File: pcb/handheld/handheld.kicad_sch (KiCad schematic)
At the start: 0 parts

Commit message: Picked some components
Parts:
- added J1: USB_C_Receptacle, symbol Connector:USB_C_Receptacle
- added U1: ESP32-S3-WROOM-1, RF_Module:ESP32-S3-WROOM-1, symbol RF_Module:ESP32-S3-WROOM-1
- added U2: AMS1117-3.3, Package_TO_SOT_SMD:SOT-223-3_TabPin2, symbol Regulator_Linear:AMS1117-3.3
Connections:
- new net: U1.1 (GND), U1.40 (GND), U1.41 (GND)
- new net: J1.A1 (GND), J1.A12 (GND), J1.B1 (GND), J1.B12 (GND)
- new net: J1.A4 (VBUS), J1.A9 (VBUS), J1.B4 (VBUS), J1.B9 (VBUS)

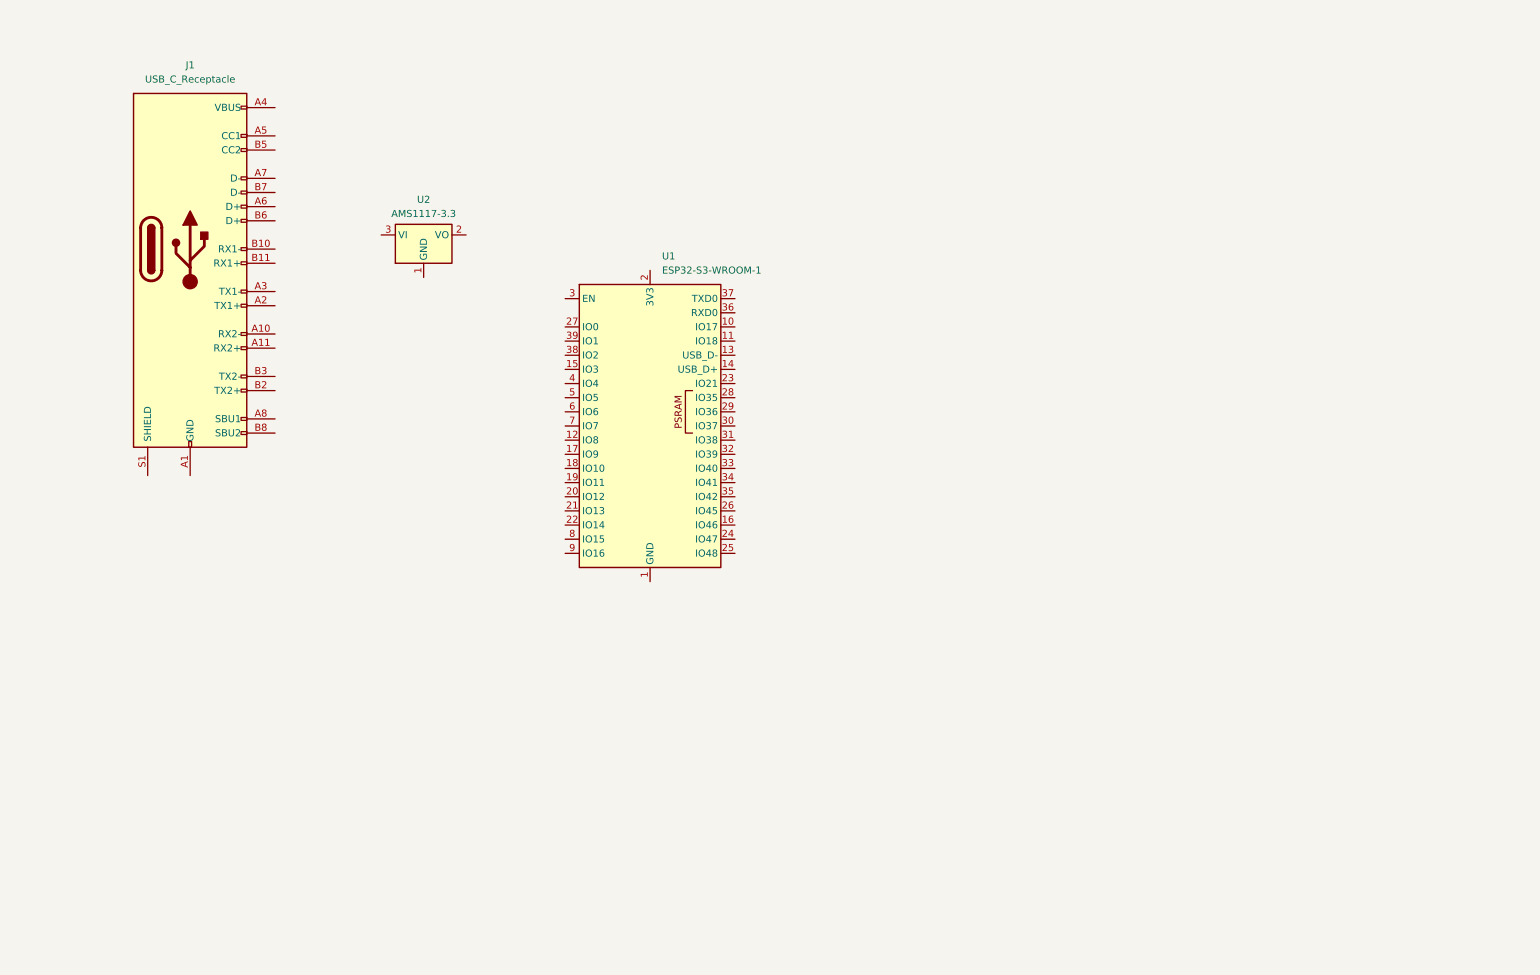
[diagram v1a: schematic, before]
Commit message: Added stuff from website
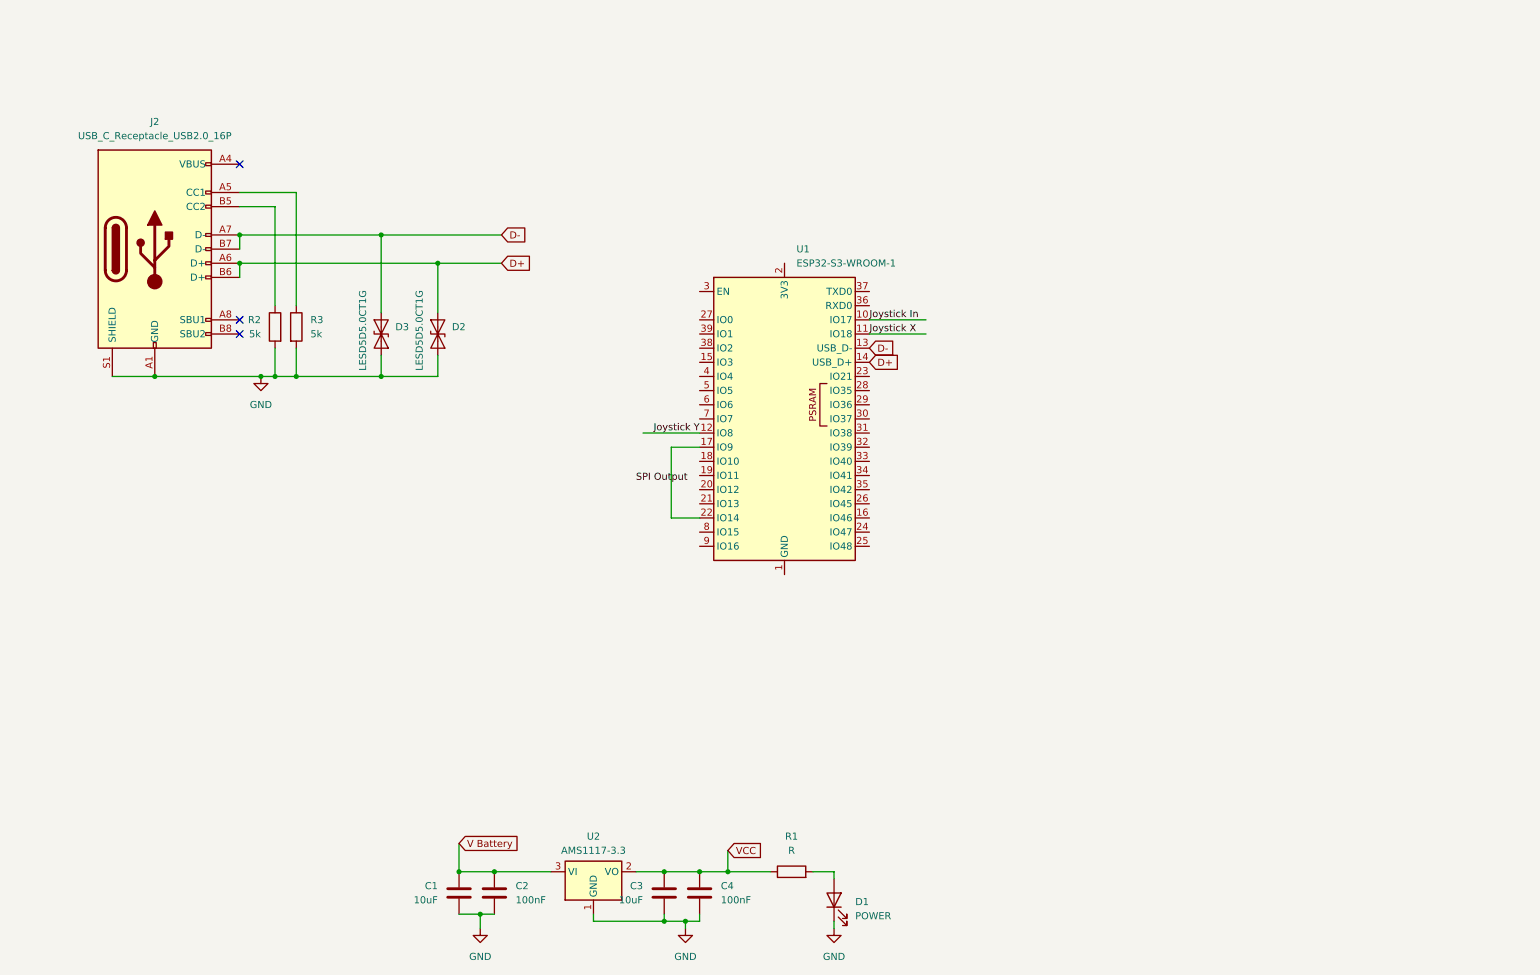
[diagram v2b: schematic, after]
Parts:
- removed J1: USB_C_Receptacle, symbol Connector:USB_C_Receptacle
- added C1, C3: 10uF, symbol Device:C
- added C2, C4: 100nF, symbol Device:C
- added D1: POWER, symbol Device:LED
- added D2, D3: LESD5D5.0CT1G, Diode_SMD:D_SOD-523, symbol Diode:ESD131-B1-W0201
- added J2: USB_C_Receptacle_USB2.0_16P, symbol Connector:USB_C_Receptacle_USB2.0_16P
- added R1: R, symbol Device:R
- added R2, R3: 5k, symbol Device:R
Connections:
- net Joystick In: now reaches U1.10 (IO17)
- net Joystick X: now reaches U1.11 (IO18)
- net Joystick Y: now reaches U1.12 (IO8)
- net D-: now reaches U1.13 (USB_D-)
- net D-: now also D3.2 (A2), J2.A7 (D-), J2.B7 (D-)
- net D+: now reaches U1.14 (USB_D+)
- net D+: now also D2.2 (A2), J2.A6 (D+), J2.B6 (D+)
- net at U1.17 (IO9): now also U1.22 (IO14)
- net GND: now reaches U2.1 (GND)
- net GND: now also C1.2, C2.2, C3.2, C4.2, D1.1 (K), D2.1 (A1), D3.1 (A1), J2.A1 (GND), J2.A12 (GND), J2.B1 (GND), J2.B12 (GND), J2.S1 (SHIELD), R2.2, R3.2
- net VCC: now reaches U2.2 (VO)
- net VCC: now also C3.1, C4.1, R1.1
- net V Battery: now reaches U2.3 (VI)
- net V Battery: now also C1.1, C2.1
- new net: J2.A5 (CC1), R3.1
- new net: D1.2 (A), R1.2
- new net: J2.A4 (VBUS), J2.A9 (VBUS), J2.B4 (VBUS), J2.B9 (VBUS)
- new net: J2.B5 (CC2), R2.1
- no-connect marks 0 -> 3
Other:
- moved on the sheet: U1, U2

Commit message: Update handheld.kicad_sch
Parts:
- added C5: 10uF, symbol Device:C
- added C6, C8, C9: 100nF, symbol Device:C
- added C7: 1uF, symbol Device:C
- added J1: Display Output, symbol Connector_Generic:Conn_01x14
- added R4, R6: R, symbol Device:R
- added R5: 10k, symbol Device:R
- added SW1: PLACEHOLDER, Button_Switch_SMD:Nidec_Copal_CAS-120A, symbol Switch:SW_Nidec_CAS-120A1
- added SW2, SW3: SW_Push, symbol Switch:SW_Push
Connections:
- net GND: now also U1.1 (GND), U1.40 (GND), U1.41 (GND), C5.2, C6.2, C7.2, C8.2, C9.2, J1.2 (Pin_2), R4.1, SW2.2, SW3.2
- net V Battery: now also SW1.3 (A); no longer C1.1, C2.1, U2.3 (VI)
- net VCC: now also U1.2 (3V3), C5.1, C6.1, J1.1 (Pin_1), R5.1, R6.1
- net at U1.17 (IO9): no longer U1.22 (IO14)
- net CS: now reaches U1.18 (IO10)
- net CS: now also J1.3 (Pin_3)
- net SDI(MOSI): now reaches U1.19 (IO11)
- net SDI(MOSI): now also J1.6 (Pin_6)
- net SCK: now reaches U1.20 (IO12)
- net SCK: now also J1.7 (Pin_7)
- net SDO(MISO): now reaches U1.21 (IO13)
- net SDO(MISO): now also J1.9 (Pin_9)
- net BOOT: now reaches U1.27 (IO0)
- net BOOT: now also C9.1, R6.2, SW3.1
- net RESET: now reaches U1.3 (EN)
- net RESET: now also C7.1, C8.1, J1.4 (Pin_4), R5.2, SW2.1
- new net: R4.2, SW1.1 (C)
- new net: C1.1, C2.1, SW1.2 (B), U2.3 (VI)
- new net DC/RS: J1.5 (Pin_5)
- new net LED: J1.8 (Pin_8)
- new net T_CLK: J1.10 (Pin_10)
- new net T_CS: J1.11 (Pin_11)
- new net T_DIN: J1.12 (Pin_12)
- new net T_DO: J1.13 (Pin_13)
- new net T_IRQ: J1.14 (Pin_14)
- no-connect marks 3 -> 8

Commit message: Schematic mostly done???
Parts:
- added J3: Speaker ~(3W, 8R), symbol Connector_Generic:Conn_01x02
- added J4: UART (Just in case?), symbol Connector_Generic:Conn_01x02
- added Q1: MMBT3904, Package_TO_SOT_SMD:SOT-23, symbol Transistor_BJT:MMBT3904
- added R7: R_Variable ~1k, symbol Device:R_Variable
- added R8: 10k, symbol Device:R
- added R9: 330, symbol Device:R
- added SW4: Push Button, symbol Switch:SW_Push
- R6: value R -> 10k
- SW2: value SW_Push -> Reset Button
- SW3: value SW_Push -> Boot Button
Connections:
- net DC/RS: now also U1.22 (IO14)
- net GND: now also J3.2 (Pin_2), Q1.2 (E), R8.2
- net LED: now also U1.7 (IO7)
- net RESET: now also U1.17 (IO9)
- net T_CLK: now also U1.23 (IO21)
- net T_CS: now also U1.9 (IO16)
- net T_DIN: now also U1.24 (IO47)
- net T_DO: now also U1.25 (IO48)
- net T_IRQ: now also U1.8 (IO15)
- net VCC: now also SW4.2
- net Speaker: now reaches U1.31 (IO38)
- net Speaker: now also R7.2
- net at U1.36 (RXD0): now also J4.2 (Pin_2)
- net at U1.37 (TXD0): now also J4.1 (Pin_1)
- new net: Q1.1 (B), R7.1
- new net: R8.1, R9.1, SW4.1
- new net: J3.1 (Pin_1), Q1.3 (C)
- new net BUTTON 1: R9.2
- no-connect marks 8 -> 9
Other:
- note added: "Generic Button Layout"

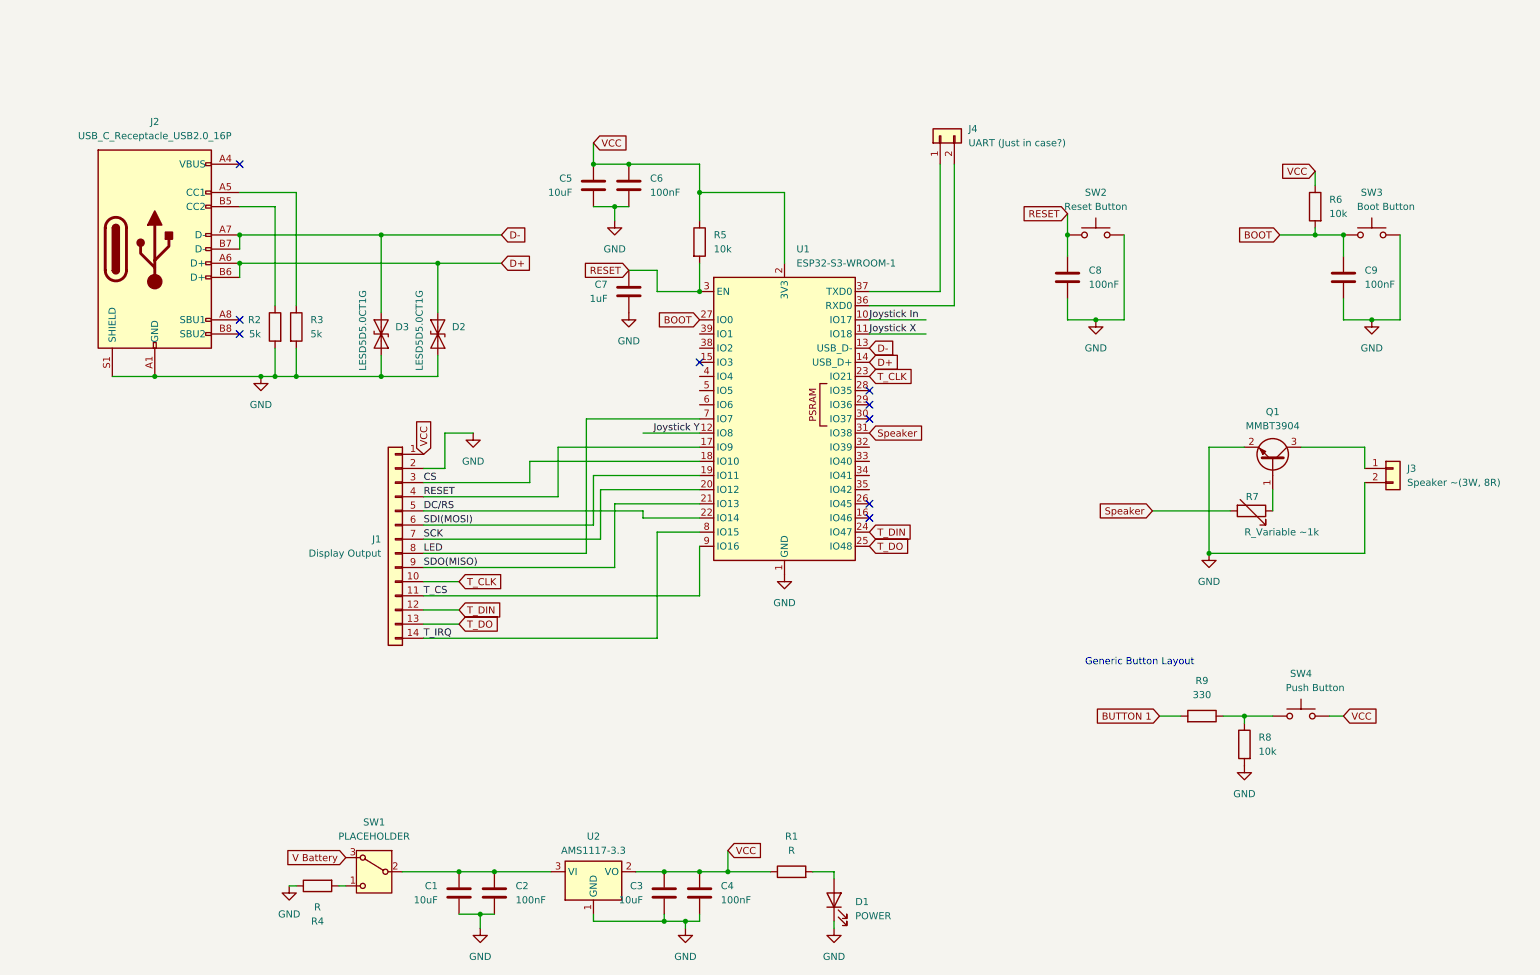
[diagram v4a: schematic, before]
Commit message: Assigned pins and finished schematic draft
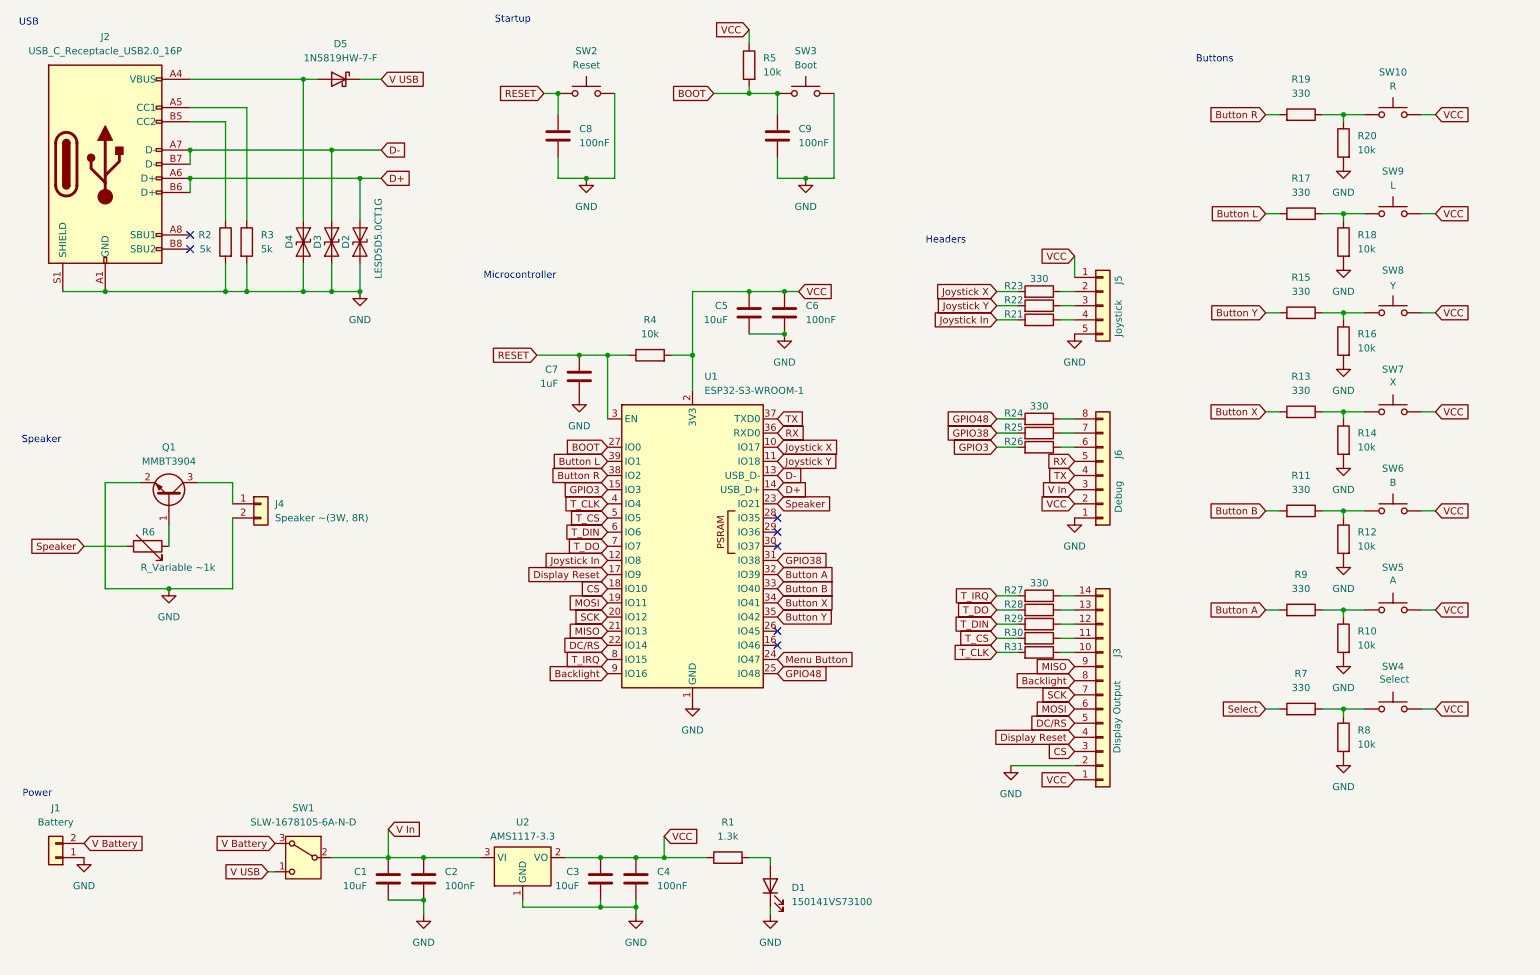
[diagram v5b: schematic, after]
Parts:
- removed J4: UART (Just in case?), symbol Connector_Generic:Conn_01x02
- removed R4: R, symbol Device:R
- added D4: LESD5D5.0CT1G, Diode_SMD:D_SOD-523, symbol Diode:ESD131-B1-W0201
- added D5: 1N5819HW-7-F, Diode_THT:D_DO-41_SOD81_P10.16mm_Horizontal, symbol Diode:1N5819
- added J1: Battery, symbol Connector_Generic:Conn_01x02
- added J5: Joystick, symbol Connector_Generic:Conn_01x05
- added J6: Debug, symbol Connector_Generic:Conn_01x08
- added R10, R12, R14, R16, R18, R20: 10k, symbol Device:R
- added R11, R13, R15, R17, R19, R21, R22, R23, R24, R25, R26, R27, R28, R29, R30, R31, R9: 330, symbol Device:R
- added SW10: R, symbol Switch:SW_Push
- added SW5: A, symbol Switch:SW_Push
- added SW6: B, symbol Switch:SW_Push
- added SW7: X, symbol Switch:SW_Push
- added SW8: Y, symbol Switch:SW_Push
- added SW9: L, symbol Switch:SW_Push
- D1: value POWER -> 150141VS73100
- R1: value R -> 1.3k
- SW1: value PLACEHOLDER -> SLW-1678105-6A-N-D
- SW2: value Reset Button -> Reset
- SW3: value Boot Button -> Boot
- SW4: value Push Button -> Select
- renumbered J1 to J3, J3 to J4, R5 to R4, R6 to R5, R7 to R6, R9 to R7
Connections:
- net GND: now also D4.1 (A1), J1.1 (Pin_1), J5.5 (Pin_5), J6.1 (Pin_1), R10.2, R12.2, R14.2, R16.2, R18.2, R20.2
- net Joystick In: now also U1.12 (IO8), R21.2; no longer U1.10 (IO17)
- net Joystick X: now also U1.10 (IO17), R23.2; no longer U1.11 (IO18)
- net Joystick Y: now also U1.11 (IO18), R22.2; no longer U1.12 (IO8)
- net RESET: now also R4.1; no longer J3.4 (Pin_4), R4.2, U1.17 (IO9)
- net Speaker: now also U1.23 (IO21); no longer U1.31 (IO38)
- net T_CLK: now also U1.4 (IO4), R31.2; no longer J3.10 (Pin_10), U1.23 (IO21)
- net T_CS: now also U1.5 (IO5), R30.2; no longer J3.11 (Pin_11), U1.9 (IO16)
- net T_DIN: now also U1.6 (IO6), R29.2; no longer J3.12 (Pin_12), U1.24 (IO47)
- net T_DO: now also U1.7 (IO7), R28.2; no longer J3.13 (Pin_13), U1.25 (IO48)
- net T_IRQ: now also R27.2; no longer J3.14 (Pin_14)
- net V Battery: now also J1.2 (Pin_2)
- net VCC: now also R4.2, J5.1 (Pin_1), J6.2 (Pin_2), SW10.2, SW5.2, SW6.2, SW7.2, SW8.2, SW9.2; no longer R4.1
- net GPIO3: now reaches U1.15 (IO3)
- net GPIO3: now also R26.2
- net Button A: now reaches U1.32 (IO39)
- net Button A: now also R9.2
- net Button B: now reaches U1.33 (IO40)
- net Button B: now also R11.2
- net Button X: now reaches U1.34 (IO41)
- net Button X: now also R13.2
- net Button Y: now reaches U1.35 (IO42)
- net Button Y: now also R15.2
- net RX: now reaches U1.36 (RXD0)
- net RX: now also J6.5 (Pin_5)
- net TX: now reaches U1.37 (TXD0)
- net TX: now also J6.4 (Pin_4)
- net Button R: now reaches U1.38 (IO2)
- net Button R: now also R19.2
- net Button L: now reaches U1.39 (IO1)
- net Button L: now also R17.2
- net V USB: now reaches SW1.1 (C)
- net V USB: now also D5.1 (K)
- net V In: now reaches C1.1, C2.1, SW1.2 (B), U2.3 (VI)
- net V In: now also J6.3 (Pin_3)
- net at J2.A4 (VBUS), J2.A9 (VBUS), J2.B4 (VBUS)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: now also D4.2 (A2), D5.2 (A)
- net BUTTON 1 renamed Select
- net LED renamed Backlight
- net Backlight: now also U1.9 (IO16); no longer U1.7 (IO7)
- net SDI(MOSI) renamed MOSI
- net SDO(MISO) renamed MISO
- new net: J3.13 (Pin_13), R28.1
- new net: R15.1, R16.1, SW8.1
- new net: R13.1, R14.1, SW7.1
- new net: R19.1, R20.1, SW10.1
- new net: R10.1, R9.1, SW5.1
- new net: J6.8 (Pin_8), R24.1
- new net: J5.3 (Pin_3), R22.1
- new net: R11.1, R12.1, SW6.1
- new net: R17.1, R18.1, SW9.1
- new net: J6.7 (Pin_7), R25.1
- new net: J3.10 (Pin_10), R31.1
- new net: J3.11 (Pin_11), R30.1
- new net: J3.12 (Pin_12), R29.1
- new net: J3.14 (Pin_14), R27.1
- new net: J6.6 (Pin_6), R26.1
- new net: J5.2 (Pin_2), R23.1
- new net: J5.4 (Pin_4), R21.1
- new net Display Reset: J3.4 (Pin_4), U1.17 (IO9)
- new net GPIO38: R25.2, U1.31 (IO38)
- new net GPIO48: R24.2, U1.25 (IO48)
- new net Menu Button: U1.24 (IO47)
- no-connect marks 9 -> 7
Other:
- note added: "Buttons"
- note added: "Headers"
- note added: "Microcontroller"
- note added: "Power"
- note added: "Speaker"
- note added: "Startup"
- note added: "USB"
- note removed: "Generic Button Layout"
- moved on the sheet: C1, C2, C3, C4, C5, C6, C7, C8, C9, D1, D2, D3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
